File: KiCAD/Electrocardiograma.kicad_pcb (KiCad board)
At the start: 2 copper layers, 39 parts, among them J1 Screw_Terminal_01x02, J3 AudioJack4, SW1 SW_DPST_x2, U1 INA128, U2 TL072, U5 TL074

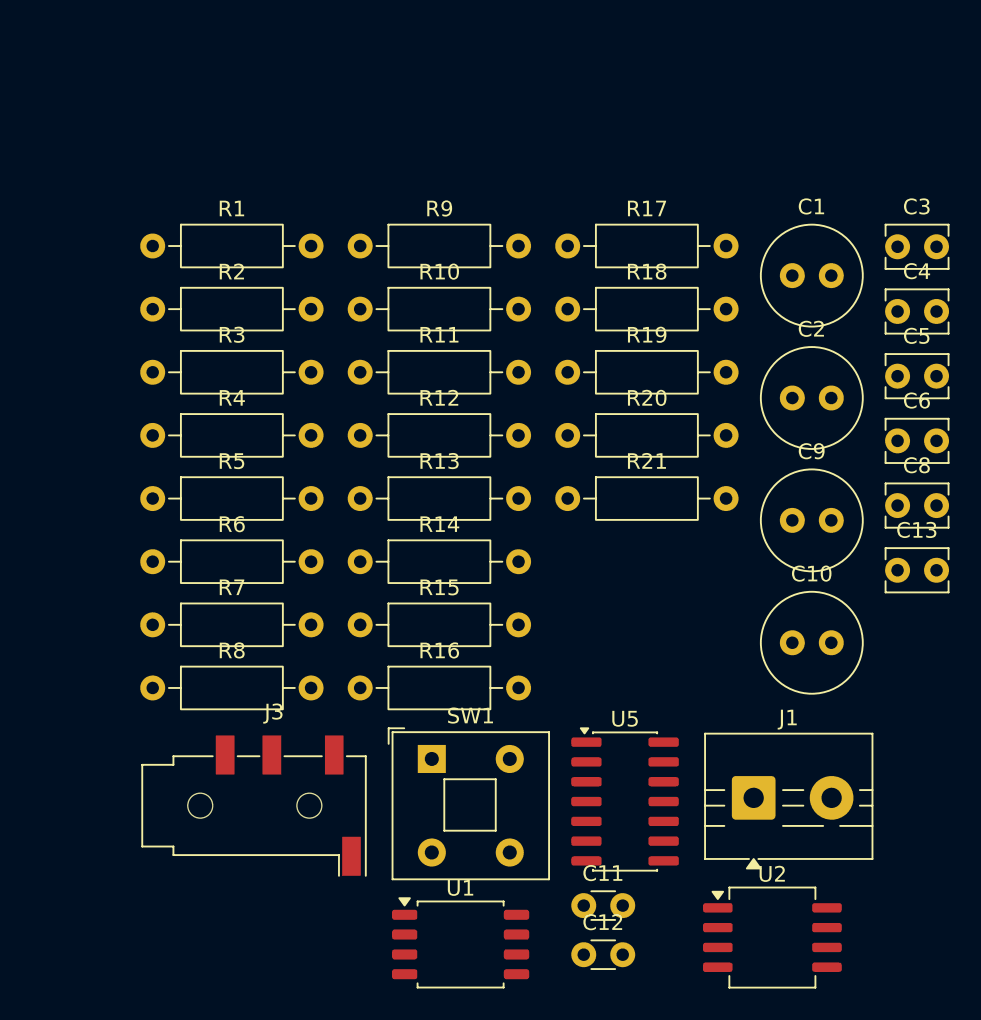
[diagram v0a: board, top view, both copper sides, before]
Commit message: footprints resistencias
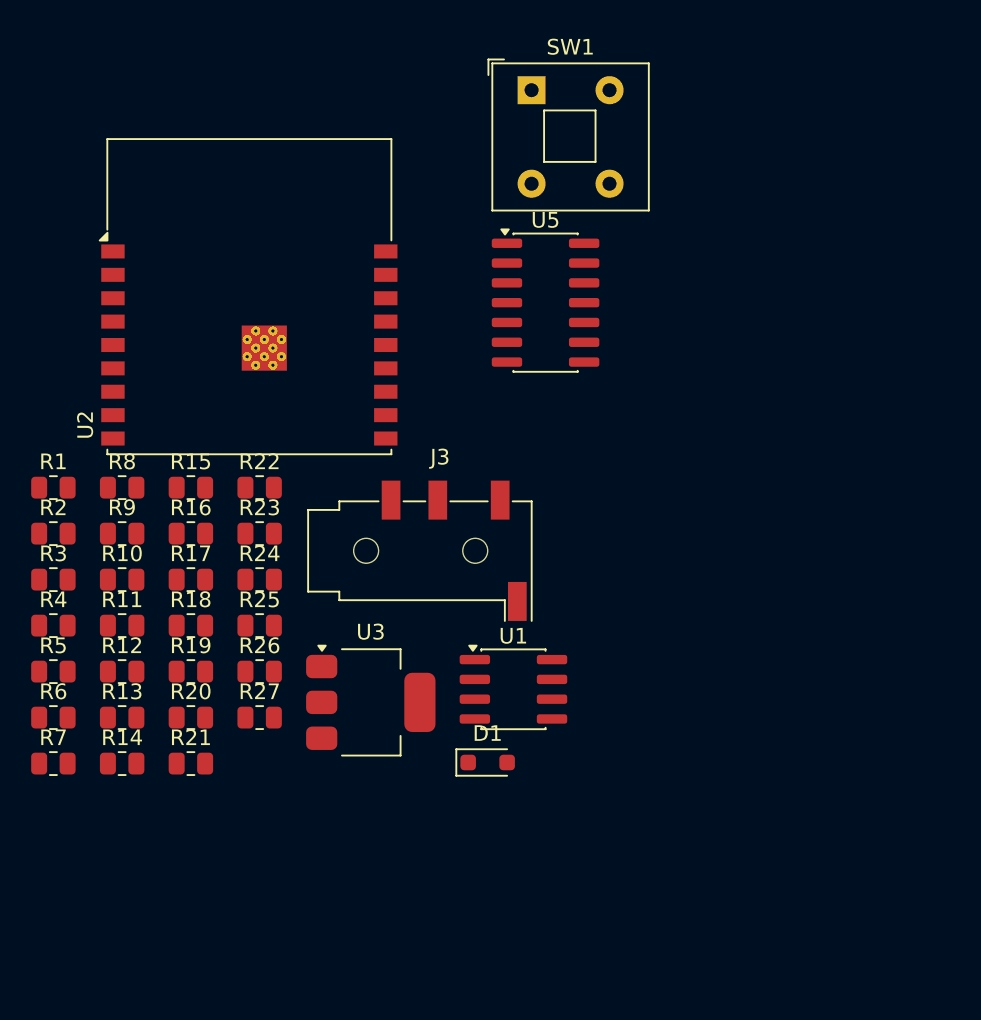
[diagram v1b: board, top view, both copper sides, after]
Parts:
- removed C1, C2: 10uF, Capacitor_THT:C_Radial_D6.3mm_H5.0mm_P2.50mm
- removed C10, C9: 10u, Capacitor_THT:C_Radial_D6.3mm_H5.0mm_P2.50mm
- removed C11, C12: 10n, Capacitor_THT:C_Disc_D3.0mm_W1.6mm_P2.50mm
- removed C13, C3, C4, C5, C6, C8: 100n, Capacitor_THT:C_Disc_D3.8mm_W2.6mm_P2.50mm
- removed J1: Screw_Terminal_01x02, TerminalBlock:TerminalBlock_MaiXu_MX126-5.0-02P_1x02_P5.00mm
- added D1: D_TVS_Dual_AAC, Diode_SMD:D_SOD-323_HandSoldering, F.Cu at (55.6, 66.7)
- added R22: 100K, Resistor_SMD:R_0805_2012Metric, F.Cu at (40.9, 49.0)
- added R23: 100K, Resistor_SMD:R_0805_2012Metric, F.Cu at (40.9, 52.0)
- added R24: 33K, Resistor_SMD:R_0805_2012Metric, F.Cu at (40.9, 54.9)
- added R25: 330k, Resistor_SMD:R_0805_2012Metric, F.Cu at (40.9, 57.9)
- added R26: 1k, Resistor_SMD:R_0805_2012Metric, F.Cu at (40.9, 60.8)
- added R27: 1k, Resistor_SMD:R_0805_2012Metric, F.Cu at (40.9, 63.8)
- added U3: AMS1117-3.3, Package_TO_SOT_SMD:SOT-223-3_TabPin2, F.Cu at (48.1, 62.8)
- R1, R2: value 470 -> 510; footprint Resistor_THT:R_Axial_DIN0207_L6.3mm_D2.5mm_P10.16mm_Horizontal -> Resistor_SMD:R_0805_2012Metric
- R10, R11, R14, R15, R16, R17, R18, R19, R20, R21, R4, R5, R6, R7, R8, R9: footprint Resistor_THT:R_Axial_DIN0207_L6.3mm_D2.5mm_P10.16mm_Horizontal -> Resistor_SMD:R_0805_2012Metric
- R12: value 10K -> 100K; footprint Resistor_THT:R_Axial_DIN0207_L6.3mm_D2.5mm_P10.16mm_Horizontal -> Resistor_SMD:R_0805_2012Metric
- R13: value 10K -> 51; footprint Resistor_THT:R_Axial_DIN0207_L6.3mm_D2.5mm_P10.16mm_Horizontal -> Resistor_SMD:R_0805_2012Metric
- R3: value 33k -> 51; footprint Resistor_THT:R_Axial_DIN0207_L6.3mm_D2.5mm_P10.16mm_Horizontal -> Resistor_SMD:R_0805_2012Metric
- U1: value INA128 -> INA823DT; footprint Package_SO:SOIC-8_5.3x5.3mm_P1.27mm -> Package_SO:SOIC-8_3.9x4.9mm_P1.27mm
- U2: value TL072 -> ESP32-C3-WROOM-02; footprint Package_SO:SOIC-8_5.3x6.2mm_P1.27mm -> RF_Module:ESP32-C3-WROOM-02
- U5: value TL074 -> TLV4888
- moved U2 50.7 mm to (40.3, 39.9)
- moved SW1 43.4 mm to (58.4, 23.5)
- moved U5 32.4 mm to (59.3, 37.2)
- moved R17 32.3 mm to (36.5, 54.9)
- moved R18 31.6 mm to (36.5, 57.9)
- moved R19 30.9 mm to (36.5, 60.8)
- moved R20 30.2 mm to (36.5, 63.8)
- moved R21 29.5 mm to (36.5, 66.7)
- moved R9 23.9 mm to (32.1, 52.0)
- moved R10 23.1 mm to (32.1, 54.9)
- moved R11 22.3 mm to (32.1, 57.9)
- moved R12 21.5 mm to (32.1, 60.8)
- moved R13 20.8 mm to (32.1, 63.8)
- moved R14 20.0 mm to (32.1, 66.7)
- moved J3 19.5 mm to (52.5, 53.1)
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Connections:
- J3 pad R1: Net-(U2B--) -> Net-(U4A--)
- R1 pad 2: Net-(U2B-+) -> Net-(U4A-+)
- R11 pad 1: /N50Hz_out -> Net-(U5B--)
- R13 pad 1: Net-(U5D-+) -> Net-(R13-Pad1)
- R13 pad 2: Net-(R13-Pad2) -> unconnected-(R13-Pad2)
- R16 pad 1: Net-(U5A--) -> -BATT
- R16 pad 2: GND -> Net-(U4C-+)
- R18 pad 1: /N50Hz_out -> Net-(U4C-+)
- R18 pad 2: Net-(C11-Pad1) -> +BATT
- R2 pad 1: Net-(U2B-+) -> Net-(U4A-+)
- R20 pad 1: Net-(U5C--) -> GND
- R20 pad 2: GND -> Net-(U5C--)
- R3 pad 1: Net-(U2A--) -> unconnected-(R3-Pad1)
- R3 pad 2: Net-(U2B--) -> Net-(R13-Pad1)
- R4 pad 2: Net-(U2A--) -> Net-(U4B--)
- U2 pad 1: Net-(R4-Pad1) -> +3.3V
- U2 pad 2: Net-(U2A--) -> +3.3V
- U2 pad 3: GND -> unconnected-(U2-IO4-Pad3)
- U2 pad 4: -BATT -> unconnected-(U2-IO5-Pad4)
- U2 pad 5: Net-(U2B-+) -> unconnected-(U2-IO6-Pad5)
- U2 pad 6: Net-(U2B--) -> unconnected-(U2-IO7-Pad6)
- U2 pad 7: Net-(U2B--) -> unconnected-(U2-IO8-Pad7)
- U2 pad 8: +BATT -> unconnected-(U2-IO9-Pad8)
- U5 pad 14: Net-(R13-Pad2) -> Net-(R25-Pad2)

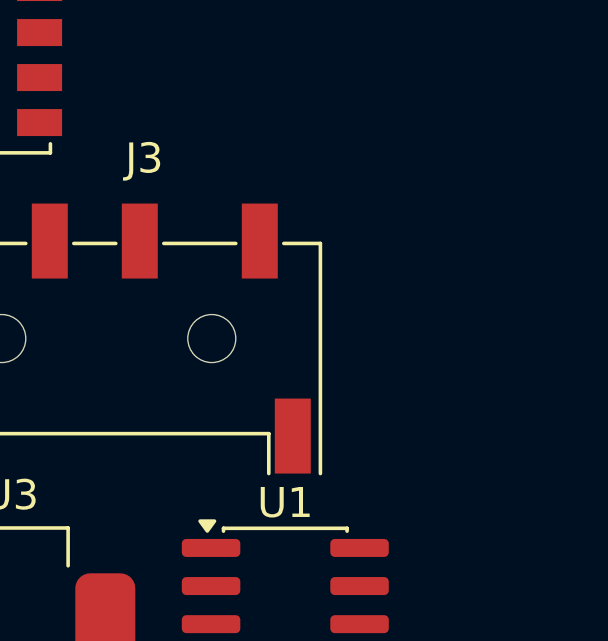
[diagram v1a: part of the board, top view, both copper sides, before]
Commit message: Configuración de programación ESP32-C3
añadí las resistencias que se necesitan para establecer el boot

Ademas separé las etapas del esquematico
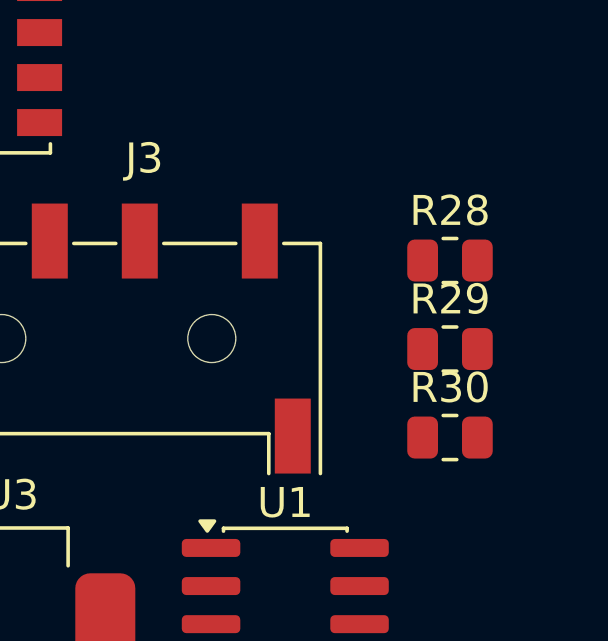
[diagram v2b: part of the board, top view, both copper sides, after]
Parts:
- added R28: 10K, Resistor_SMD:R_0805_2012Metric, F.Cu at (62.7, 50.5)
- added R29: 10K, Resistor_SMD:R_0805_2012Metric, F.Cu at (62.7, 53.4)
- added R30: 10K, Resistor_SMD:R_0805_2012Metric, F.Cu at (62.7, 56.4)
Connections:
- U2 pad 13: unconnected-(U2-IO18-Pad13) -> /USB_D-
- U2 pad 14: unconnected-(U2-IO19-Pad14) -> /USB_D+
- U2 pad 15: unconnected-(U2-IO3-Pad15) -> /ADC_3
- U2 pad 17: unconnected-(U2-IO1-Pad17) -> /ADC_1
- U2 pad 18: unconnected-(U2-IO0-Pad18) -> /ADC_0
- U2 pad 2: +3.3V -> /Reset
- U2 pad 7: unconnected-(U2-IO8-Pad7) -> /Boot1
- U2 pad 8: unconnected-(U2-IO9-Pad8) -> /Boot2

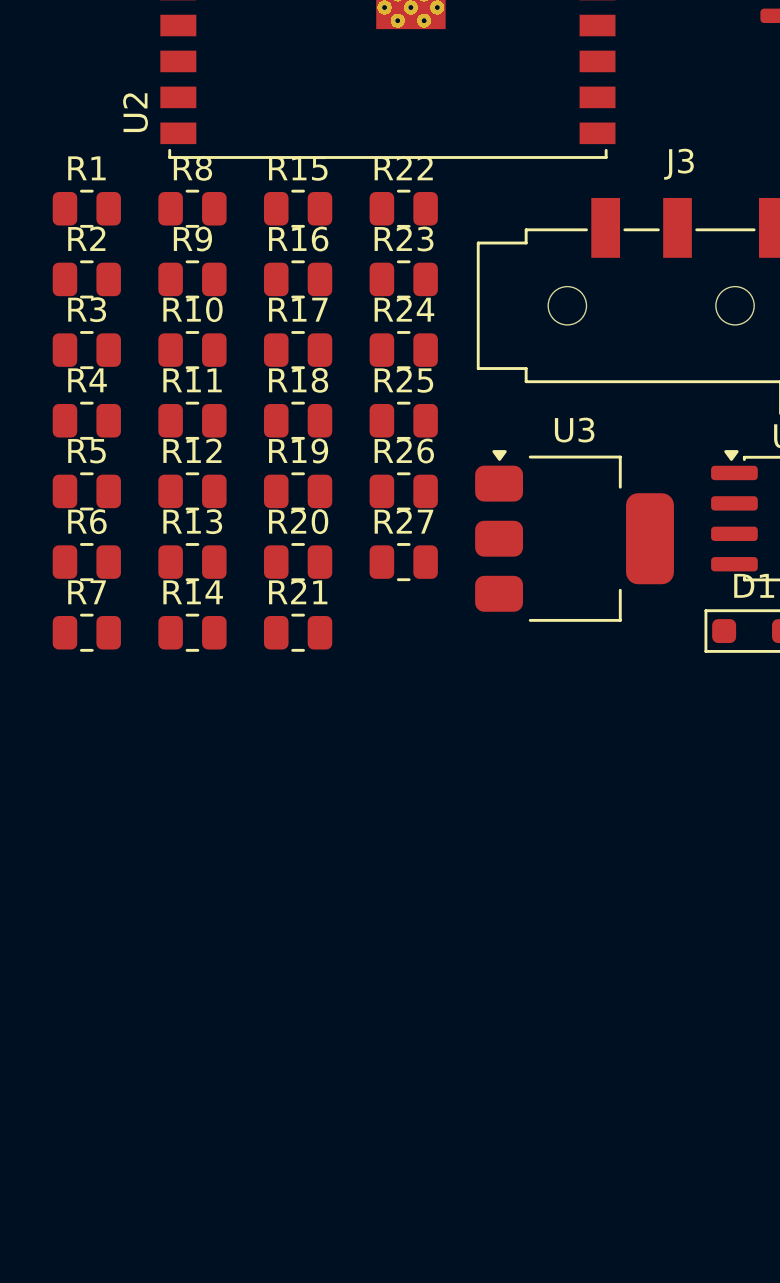
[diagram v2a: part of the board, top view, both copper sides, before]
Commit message: Update KiCAD PCB footprints and pad geometry
Replace and correct multiple footprints  across the PCB. Also add/replace a TO-252/SOT regulator footprint for TLV1117-33 with proper pad geometry and net assignments, update DigiKey/Datasheet fields and numerous UUIDs.
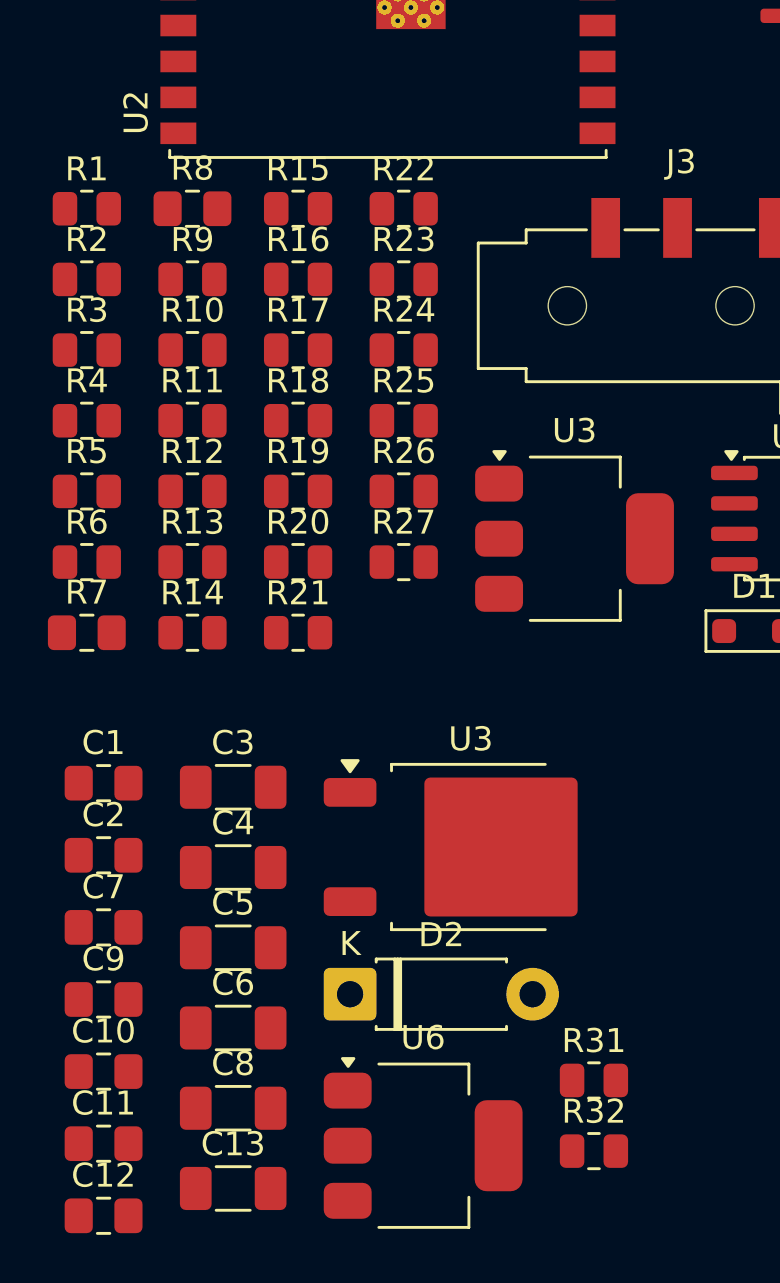
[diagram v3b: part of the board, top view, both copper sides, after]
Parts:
- added C1: 10uF, Capacitor_SMD:C_0805_2012Metric_Pad1.18x1.45mm_HandSolder, F.Cu at (28.4, 73.0)
- added C10: 10uF, Capacitor_SMD:C_0805_2012Metric_Pad1.18x1.45mm_HandSolder, F.Cu at (28.4, 85.0)
- added C11: 10n, Capacitor_SMD:C_0805_2012Metric_Pad1.18x1.45mm_HandSolder, F.Cu at (28.4, 88.1)
- added C12: 10n, Capacitor_SMD:C_0805_2012Metric_Pad1.18x1.45mm_HandSolder, F.Cu at (28.4, 91.1)
- added C13: 100n, Capacitor_SMD:C_1206_3216Metric_Pad1.33x1.80mm_HandSolder, F.Cu at (33.8, 89.9)
- added C2: 10uF, Capacitor_SMD:C_0805_2012Metric_Pad1.18x1.45mm_HandSolder, F.Cu at (28.4, 76.0)
- added C3: 100n, Capacitor_SMD:C_1206_3216Metric_Pad1.33x1.80mm_HandSolder, F.Cu at (33.8, 73.2)
- added C4: 100n, Capacitor_SMD:C_1206_3216Metric_Pad1.33x1.80mm_HandSolder, F.Cu at (33.8, 76.5)
- added C5: 100n, Capacitor_SMD:C_1206_3216Metric_Pad1.33x1.80mm_HandSolder, F.Cu at (33.8, 79.9)
- added C6: 100n, Capacitor_SMD:C_1206_3216Metric_Pad1.33x1.80mm_HandSolder, F.Cu at (33.8, 83.2)
- added C7: 10uF, Capacitor_SMD:C_0805_2012Metric_Pad1.18x1.45mm_HandSolder, F.Cu at (28.4, 79.0)
- added C8: 100n, Capacitor_SMD:C_1206_3216Metric_Pad1.33x1.80mm_HandSolder, F.Cu at (33.8, 86.6)
- added C9: 10uF, Capacitor_SMD:C_0805_2012Metric_Pad1.18x1.45mm_HandSolder, F.Cu at (28.4, 82.0)
- added D2: 1N4007, Diode_THT:D_DO-41_SOD81_P7.62mm_Horizontal, F.Cu at (38.7, 81.8)
- added R31: 120, Resistor_SMD:R_0805_2012Metric, F.Cu at (48.9, 85.4)
- added R32: 453, Resistor_SMD:R_0805_2012Metric, F.Cu at (48.9, 88.4)
- added U3: TLV1117-33, Package_TO_SOT_SMD:TO-252-2, F.Cu at (43.7, 75.7)
- added U6: TLV1117-ADJ, Package_TO_SOT_SMD:SOT-223-3_TabPin2, F.Cu at (41.7, 88.1)
- R7, R8: footprint Resistor_SMD:R_0805_2012Metric -> Capacitor_SMD:C_0805_2012Metric_Pad1.18x1.45mm_HandSolder
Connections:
- net Net-(R25-Pad2) renamed /Sensing_Out
- D1 pad 1: +BATT -> +BATT_REG
- R16 pad 1: -BATT -> -BATT_REG
- R18 pad 2: +BATT -> +6.1V
- SW1 pad 2: +BATT -> Net-(D2-A)
- U1 pad 4: -BATT -> -BATT_REG
- U1 pad 7: +BATT -> +5.0V
- U2 pad 19: -BATT -> -BATT_REG
- U2 pad 9: -BATT -> -BATT_REG
- U5 pad 11: -BATT -> -BATT_REG
- U5 pad 4: +BATT -> +6.1V

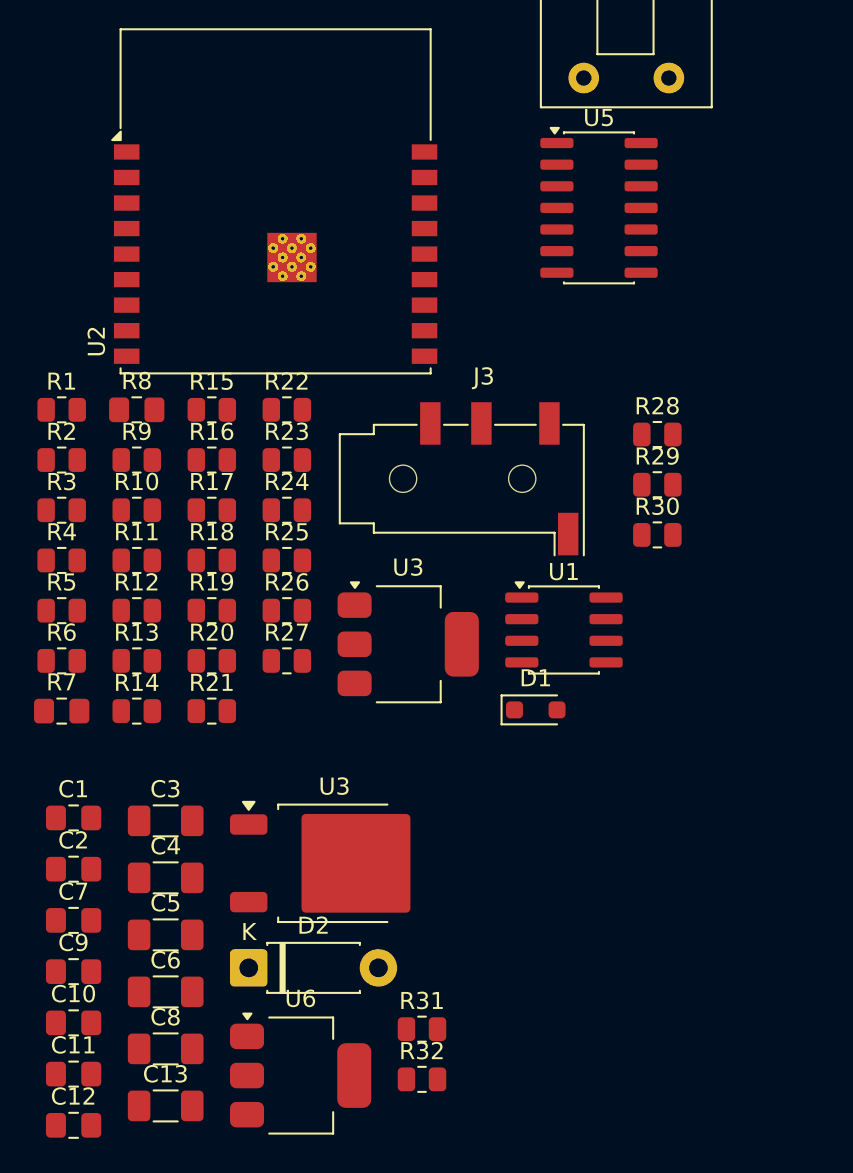
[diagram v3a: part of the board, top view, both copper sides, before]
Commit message: Fixed Diode and Resistors mistaken  Models
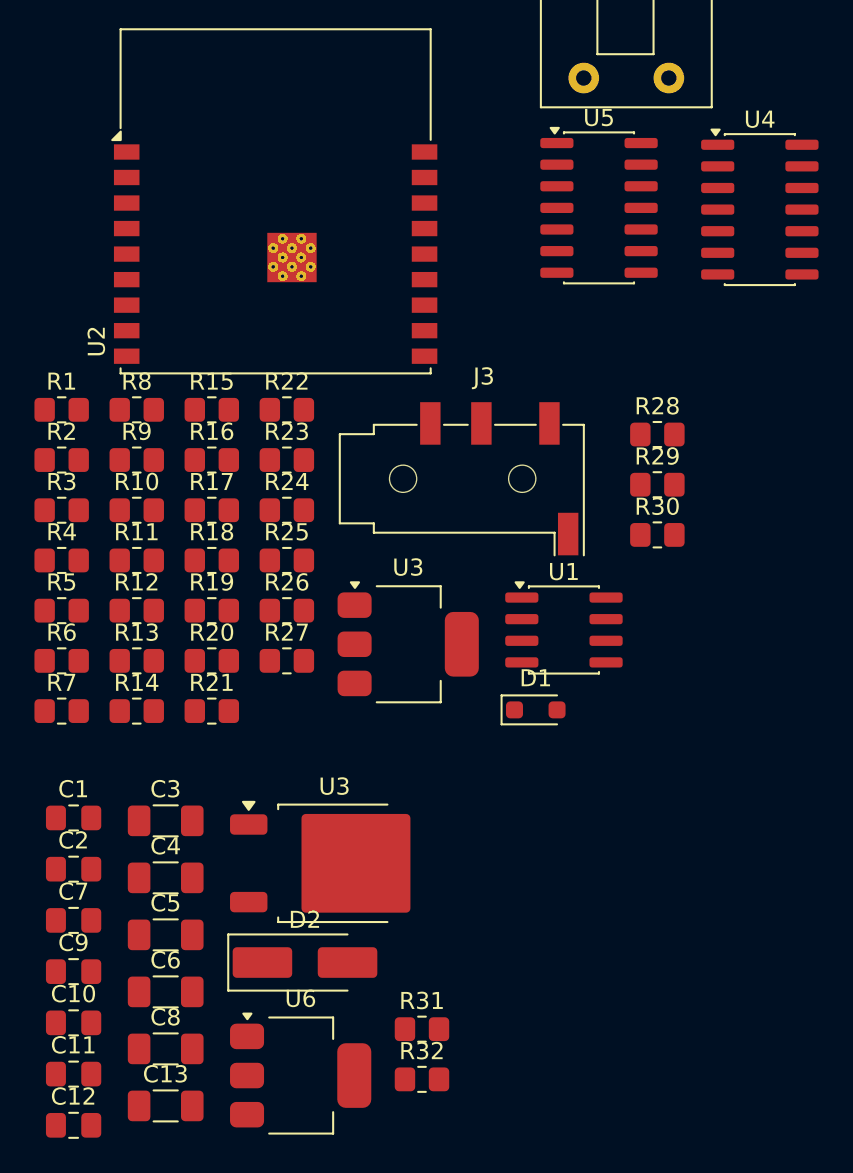
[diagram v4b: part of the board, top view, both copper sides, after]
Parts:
- added U4: TLV4888, Package_SO:SOIC-14_3.9x8.7mm_P1.27mm, F.Cu at (68.7, 37.3)
- D2: footprint Diode_THT:D_DO-41_SOD81_P7.62mm_Horizontal -> Diode_SMD:D_SMA_Handsoldering
- R1, R10, R11, R12, R13, R14, R15, R16, R17, R18, R19, R2, R20, R21, R22, R23, R24, R25, R26, R27, R28, R29, R3, R30, R31, R32, R4, R5, R6, R9: footprint Resistor_SMD:R_0805_2012Metric -> Resistor_SMD:R_0805_2012Metric_Pad1.20x1.40mm_HandSolder
- R7, R8: footprint Capacitor_SMD:C_0805_2012Metric_Pad1.18x1.45mm_HandSolder -> Resistor_SMD:R_0805_2012Metric_Pad1.20x1.40mm_HandSolder
- moved D2 3.32 mm to (42.0, 81.5)
